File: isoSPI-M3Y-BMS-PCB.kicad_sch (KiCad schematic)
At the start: 439 parts, among them J1 Screw_Terminal_01x04, J10 Screw_Terminal_01x04, J11 Screw_Terminal_01x03, J12 Screw_Terminal_01x08, J13 Conn_02x10_Odd_Even, J14 Screw_Terminal_01x04, J15 USB_C_Receptacle_USB2.0_16P, J16 Conn_01x03, J17 USB_C_Receptacle_USB2.0_16P, J18 USB_C_Receptacle_USB2.0_16P, J2 Conn_02x10_Odd_Even, J3 8P8C_LED_Shielded_x2, J5 OEM Shunt Connector, J6 349128020, J7 OEM HV Sense Connector, J8 OEM Connector, J9 Conn_01x03, K10 FC Positive, K11 FC Negative, K12 Link Negative, K13 Inverter, K14 Link Positive, K15 Link Negative, K16 FC Positive, K17 FC Negative, K18 Inverter, K9 Link Positive, Q1 CRSM034N06L2, Q2 CRSM034N06L2, Q3 CRSM034N06L2, Q5 CRSM034N06L2, SW1 TS-1187A-B-A-B, SW2 TS-1187A-B-A-B, SW3 TS-1187A-B-A-B, SW4 TS-1187A-B-A-B, U1 SN74LV1T08DBVR, U10 LTV-217-B-G, U11 RP2354B, U12 ADS1115, U13 ISO1050DUB, U15 SN74LV1T08DBVR, U16 BatMan, U17 TPS5430DDAR, U2 ISO1540, U20 LTV-217-B-G, U21 AMS1117-3.3, U22 F0505S-1WR3, U23 SN74LV1T08DBVR, U24 F0505S-1WR3, U25 SN74LV1T08DBVR, U26 SN74LV1T08DBVR, U27 RP2354B, U28 AM26LV32EIDR, U29 B0505S-3WR2, U3 INA228, U30 ISO1540, U32 SP3485EN-L/TR, U4 ISO1540, U5 LTV-217-B-G, U6 F0505S-1WR3, U7 LTV-217-B-G, U8 LTV-217-B-G, U9 LTV-217-B-G, Y1 ABM8-272-T3, Y2 ABM8-272-T3

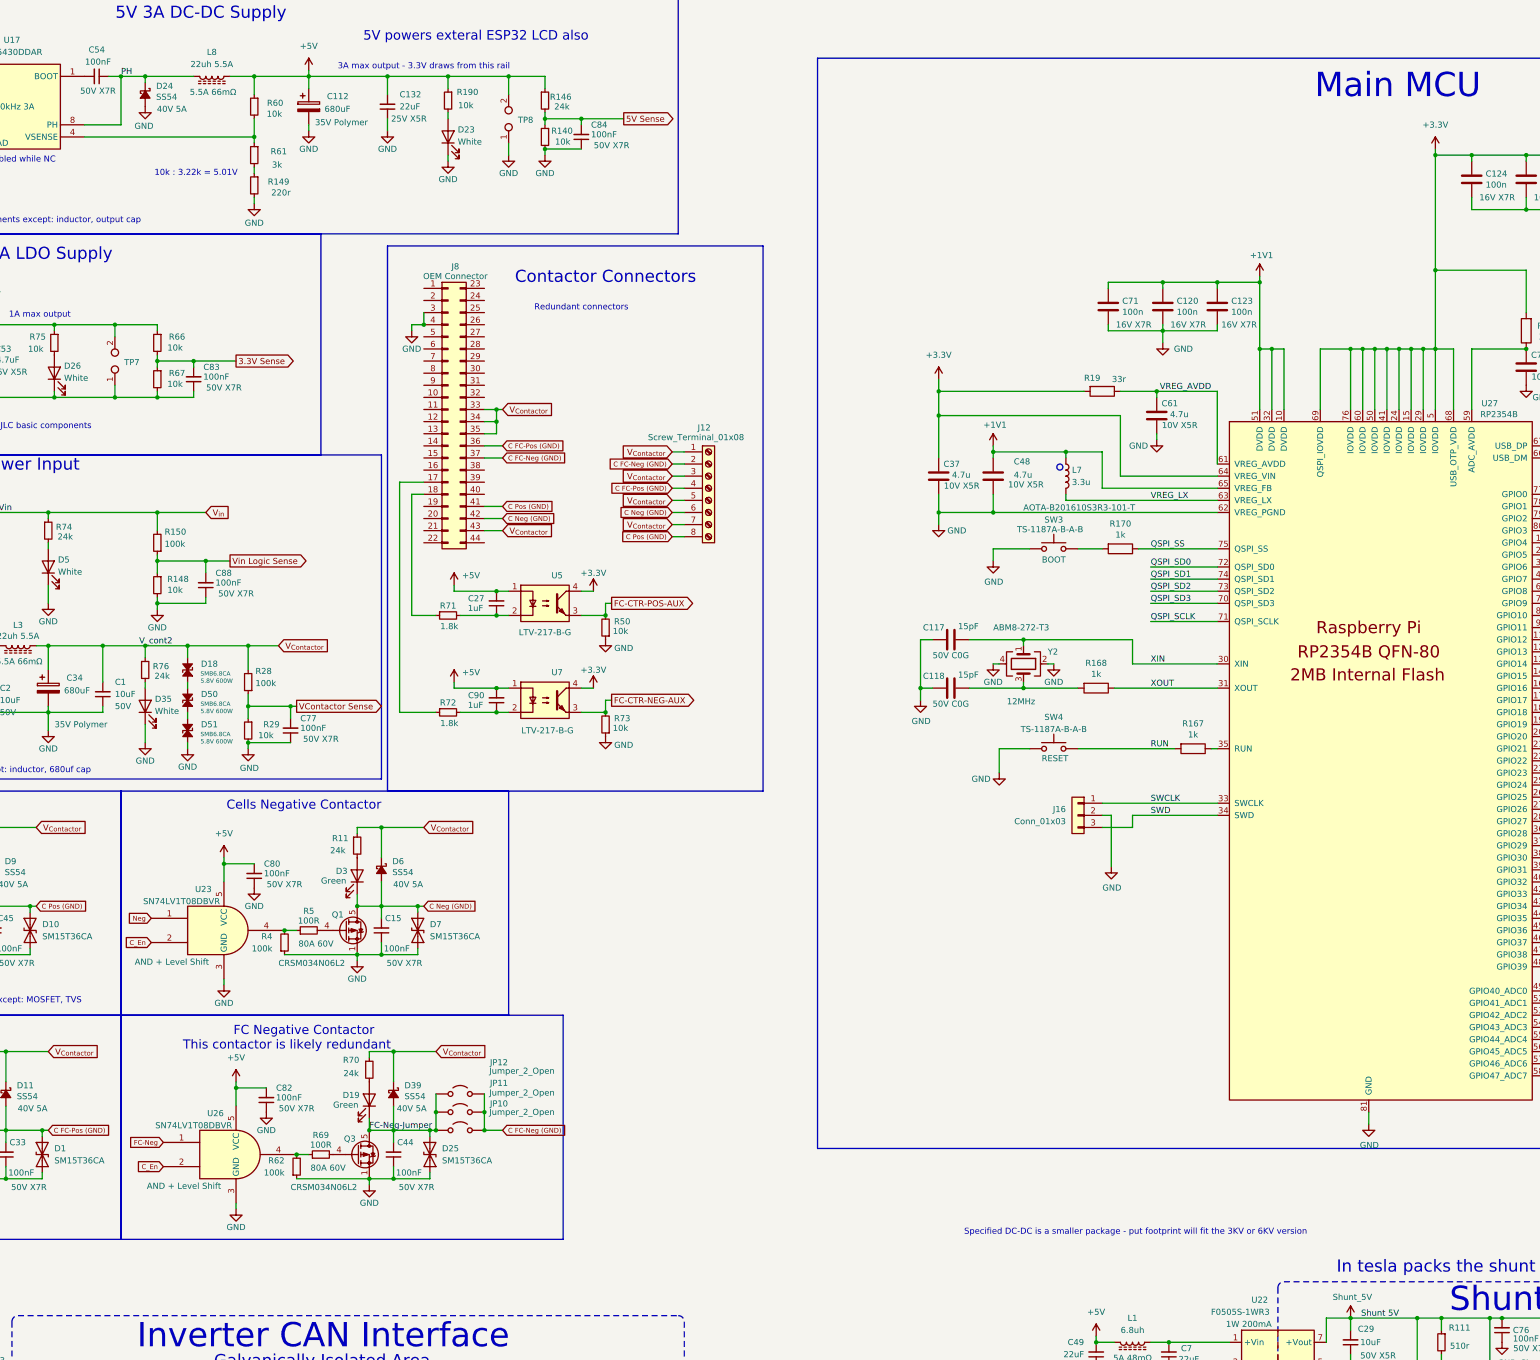
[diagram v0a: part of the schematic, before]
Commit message: routed dc-dc
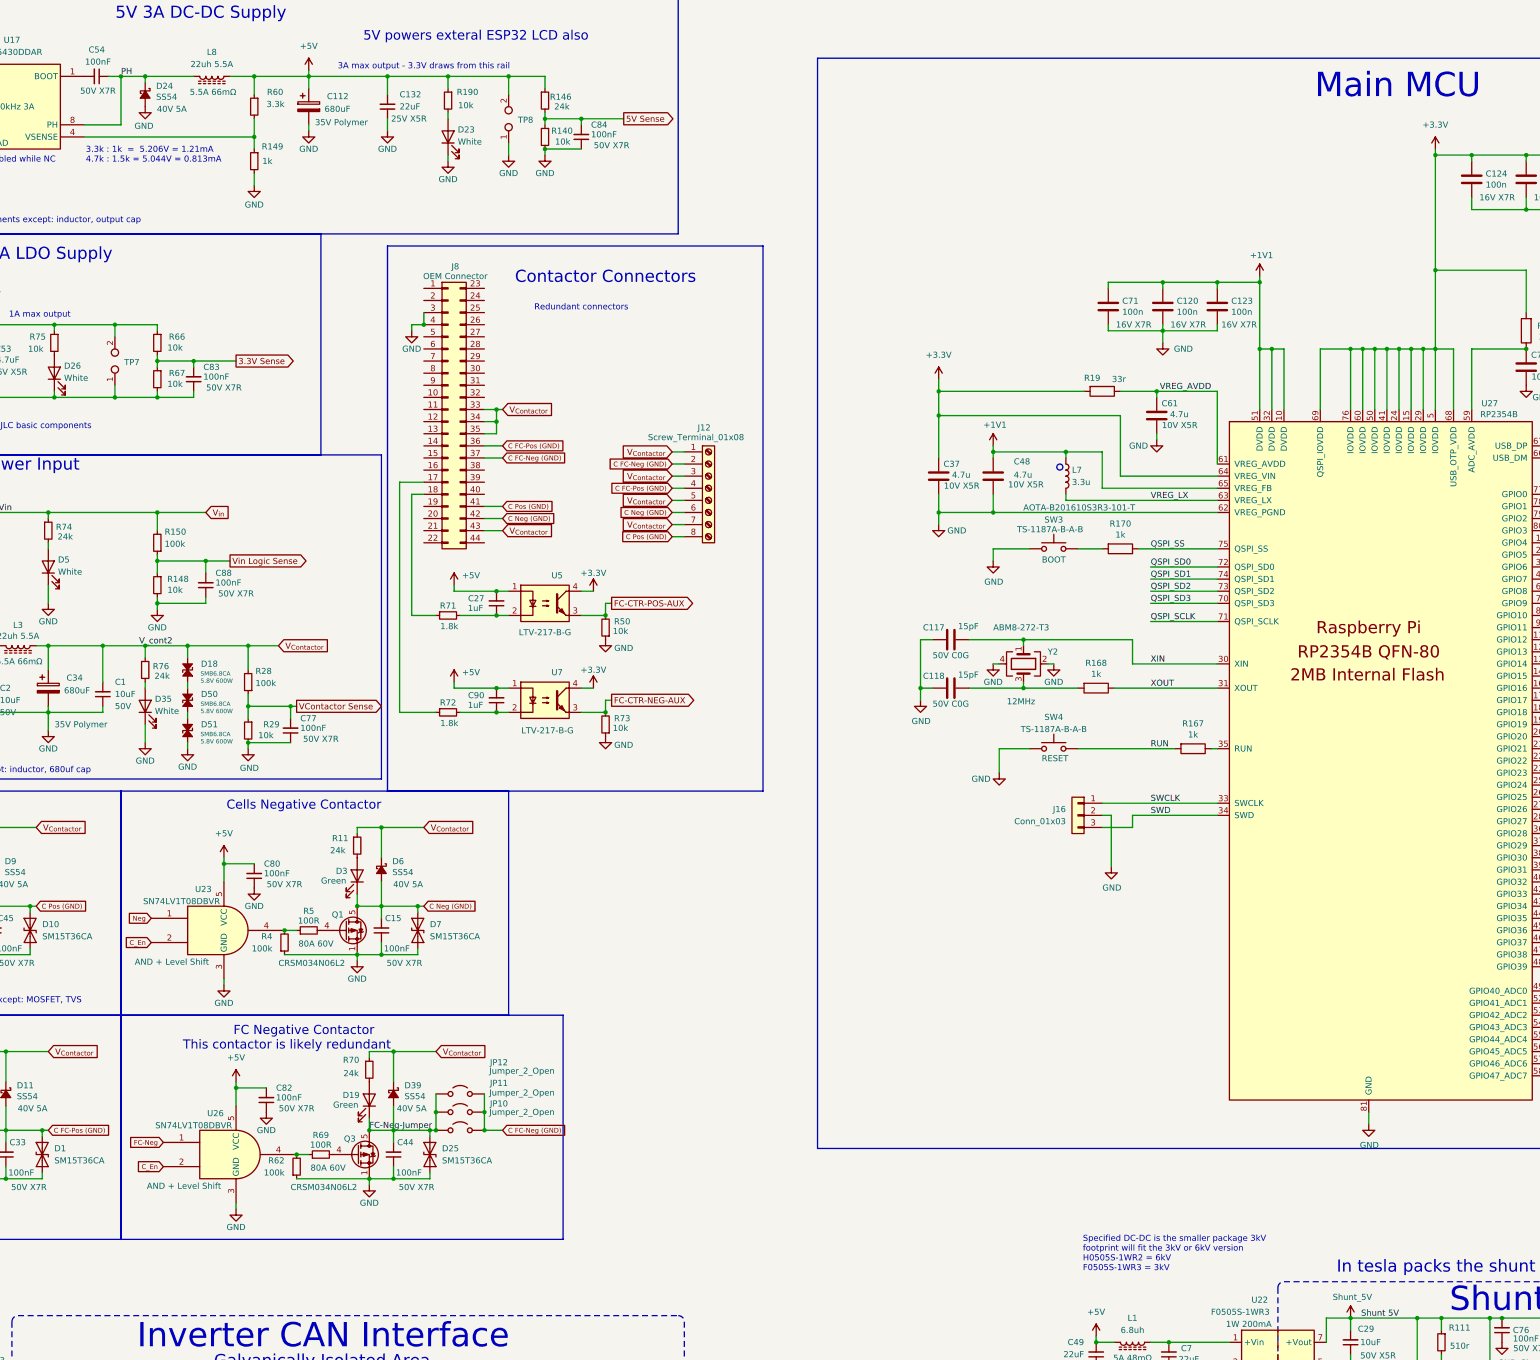
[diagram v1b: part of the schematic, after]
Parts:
- removed R61: 3k, Resistor_SMD:R_0603_1608Metric, symbol Device:R_Small
- R149: value 220r -> 1k; footprint Resistor_SMD:R_0603_1608Metric -> Resistor_SMD:R_0402_1005Metric; JLCPCB Part # C22962 -> C11702
- R60: value 10k -> 3.3k; footprint Resistor_SMD:R_0603_1608Metric -> Resistor_SMD:R_0402_1005Metric; JLCPCB Part # C25804 -> C25890
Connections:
- net at R60.2, U17.4 (VSENSE): now also R149.1
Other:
- note added: "3.3k : 1k = 5.206V = 1.21mA 4.7k : 1.5k = 5.044V = 0.813mA"
- note added: "Specified DC-DC is the smaller package 3kV footprint will fit the 3kV or 6kV version H0505S-1WR2 = 6kV F0505S-1WR3 = 3kV"
- note removed: "10k : 3.22k = 5.01V"
- note removed: "Specified DC-DC is a smaller package - put footprint will fit the 3KV or 6KV version"
- moved on the sheet: R149
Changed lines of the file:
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@@
 		)
 	)
-	(text "Specified DC-DC is a smaller package - put footprint will fit the 3KV or 6KV version"
+	(text "Specified DC-DC is the smaller package 3kV\nfootprint will fit the 3kV or 6kV version\nH0505S-1WR2 = 6kV\nF0505S-1WR3 = 3kV\n"
 		(exclude_from_sim no)
-		(at 277.114 282.448 0)
+		(at 302.006 290.068 0)
 		(effects
 			(font
@@
 		)
 	)
-	(text "10k : 3.22k = 5.01V"
+	(text "3.3k : 1k  =  5.206V = 1.21mA\n4.7k : 1.5k = 5.044V = 0.813mA"
 		(exclude_from_sim no)
-		(at 116.078 59.69 0)
+		(at 92.964 55.88 0)
 		(effects
 			(font
 				(size 1.27 1.27)
 			)
+			(justify left)
 		)
 	)
@@
 	(wire
 		(pts
-			(xy 128.27 64.77) (xy 128.27 66.04)
+			(xy 128.27 59.69) (xy 128.27 62.23)
 		)
 		(stroke
@@
 	(wire
 		(pts
-			(xy 128.27 52.07) (xy 128.27 53.34)
+			(xy 128.27 52.07) (xy 128.27 54.61)
 		)
 		(stroke
@@
 	(wire
 		(pts
-			(xy 128.27 58.42) (xy 128.27 59.69)
-		)
-		(stroke
-			(width 0)
-			(type default)
-		)
-	)
-	(wire
-		(pts
 			(xy 646.43 358.14) (xy 652.78 358.14)
 		)
@@
 	)
 	(symbol
-		(lib_id "Device:R_Small")
-		(at 128.27 55.88 0)
-		(mirror y)
-		(unit 1)
-		(exclude_from_sim no)
-		(in_bom yes)
-		(on_board yes)
-		(dnp no)
-		(property "Reference" "R61"
-			(at 135.128 55.118 0)
-			(effects
-				(font
-					(size 1.27 1.27)
-				)
-				(justify left)
-			)
-		)
-		(property "Value" "3k"
-			(at 134.112 57.912 0)
-			(effects
-				(font
-					(size 1.27 1.27)
-				)
-				(justify left)
-			)
-		)
-		(property "Footprint" "Resistor_SMD:R_0603_1608Metric"
-			(at 128.27 55.88 0)
-			(effects
-				(font
-					(size 1.27 1.27)
-				)
-				(hide yes)
-			)
-		)
-		(property "Datasheet" ""
-			(at 128.27 55.88 0)
-			(effects
-				(font
-					(size 1.27 1.27)
-				)
-				(hide yes)
-			)
-		)
-		(property "Description" ""
-			(at 128.27 55.88 0)
-			(effects
-				(font
-					(size 1.27 1.27)
-				)
-				(hide yes)
-			)
-		)
-		(property "JLCPCB Part #" "C4211"
-			(at 128.27 55.88 0)
-			(effects
-				(font
-					(size 1.27 1.27)
-				)
-				(hide yes)
-			)
-		)
-		(pin "1"
-		)
-		(pin "2"
-		)
-		(instances
-			(project "bms"
-				(path "/5d962221-5e0a-481f-afc5-67c7ec101fc1"
-					(reference "R61")
-					(unit 1)
-				)
-			)
-		)
-	)
-	(symbol
 		(lib_id "Device:C_Small")
 		(at 408.94 382.27 0)
@@
 	)
 	(symbol
+		(lib_id "Device:R_Small")
+		(at 128.27 45.72 0)
+		(mirror y)
+		(unit 1)
+		(exclude_from_sim no)
+		(in_bom yes)
+		(on_board yes)
+		(dnp no)
+		(property "Reference" "R60"
+			(at 134.366 42.672 0)
+			(effects
+				(font
+					(size 1.27 1.27)
+				)
+				(justify left)
+			)
+		)
+		(property "Value" "3.3k"
+			(at 134.62 45.212 0)
+			(effects
+				(font
+					(size 1.27 1.27)
+				)
+				(justify left)
+			)
+		)
+		(property "Footprint" "Resistor_SMD:R_0402_1005Metric"
+			(at 128.27 45.72 0)
+			(effects
+				(font
+					(size 1.27 1.27)
+				)
+				(hide yes)
+			)
+		)
+		(property "Datasheet" ""
+			(at 128.27 45.72 0)
+			(effects
+				(font
+					(size 1.27 1.27)
+				)
+				(hide yes)
+			)
+		)
+		(property "Description" ""
+			(at 128.27 45.72 0)
+			(effects
+				(font
+					(size 1.27 1.27)
+				)
+				(hide yes)
+			)
+		)
+		(property "JLCPCB Part #" "C25890"
+			(at 128.27 45.72 0)
+			(effects
+				(font
+					(size 1.27 1.27)
+				)
+				(hide yes)
+			)
+		)
+		(pin "1"
+		)
+		(pin "2"
+		)
+		(instances
+			(project "isoSPI-M3Y-BMS-PCB"
+				(path "/5d962221-5e0a-481f-afc5-67c7ec101fc1"
+					(reference "R60")
+					(unit 1)
+				)
+			)
+		)
+	)
+	(symbol
 		(lib_id "power:GND")
 		(at 389.89 304.8 0)
@@
 	(symbol
 		(lib_id "power:GND")
-		(at 128.27 66.04 0)
+		(at 128.27 62.23 0)
 		(unit 1)
 		(exclude_from_sim no)
@@
 		(dnp no)
 		(property "Reference" "#PWR058"
-			(at 128.27 72.39 0)
+			(at 128.27 68.58 0)
 			(effects
 				(font
@@
 		)
 		(property "Value" "GND"
-			(at 128.27 70.104 0)
+			(at 128.27 66.294 0)
 			(effects
 				(font
@@
 		)
 		(property "Footprint" ""
-			(at 128.27 66.04 0)
+			(at 128.27 62.23 0)
 			(effects
 				(font
@@
 		)
 		(property "Datasheet" ""
-			(at 128.27 66.04 0)
+			(at 128.27 62.23 0)
 			(effects
 				(font
@@
 		)
 		(property "Description" "Power symbol creates a global label with name \"GND\" , ground"
-			(at 128.27 66.04 0)
+			(at 128.27 62.23 0)
 			(effects
 				(font
@@
 	(symbol
 		(lib_id "Device:R_Small")
-		(at 128.27 62.23 0)
+		(at 128.27 57.15 0)
 		(mirror y)
 		(unit 1)
@@
 		(dnp no)
 		(property "Reference" "R149"
-			(at 135.636 61.468 0)
+			(at 134.366 54.102 0)
 			(effects
 				(font
@@
 			)
 		)
-		(property "Value" "220r"
-			(at 135.89 63.754 0)
+		(property "Value" "1k"
+			(at 132.08 57.15 0)
 			(effects
 				(font
@@
 			)
 		)
-		(property "Footprint" "Resistor_SMD:R_0603_1608Metric"
-			(at 128.27 62.23 0)
+		(property "Footprint" "Resistor_SMD:R_0402_1005Metric"
+			(at 128.27 57.15 0)
 			(effects
 				(font
@@
 		)
 		(property "Datasheet" ""
-			(at 128.27 62.23 0)
+			(at 128.27 57.15 0)
 			(effects
 				(font
@@
 		)
 		(property "Description" ""
-			(at 128.27 62.23 0)
+			(at 128.27 57.15 0)
 			(effects
 				(font
@@
 			)
 		)
-		(property "JLCPCB Part #" "C22962"
-			(at 128.27 62.23 0)
+		(property "JLCPCB Part #" "C11702"
+			(at 128.27 57.15 0)
 			(effects
 				(font
@@
 					(unit 1)
 				)
-			)
-		)
-	)
-	(symbol
-		(lib_id "Device:R_Small")
-		(at 128.27 45.72 0)
-		(mirror y)
-		(unit 1)
-		(exclude_from_sim no)
-		(in_bom yes)
-		(on_board yes)
-		(dnp no)
-		(property "Reference" "R60"
-			(at 134.366 44.958 0)
-			(effects
-				(font
-					(size 1.27 1.27)
-				)
-				(justify left)
-			)
-		)
-		(property "Value" "10k"
-			(at 134.112 47.244 0)
-			(effects
-				(font
-					(size 1.27 1.27)
-				)
-				(justify left)
-			)
-		)
-		(property "Footprint" "Resistor_SMD:R_0603_1608Metric"
-			(at 128.27 45.72 0)
-			(effects
-				(font
-					(size 1.27 1.27)
-				)
-				(hide yes)
-			)
-		)
-		(property "Datasheet" "~"
-			(at 128.27 45.72 0)
-			(effects
-				(font
-					(size 1.27 1.27)
-				)
-				(hide yes)
-			)
-		)
-		(property "Description" "Resistor, small symbol"
-			(at 128.27 45.72 0)
-			(effects
-				(font
-					(size 1.27 1.27)
-				)
-				(hide yes)
-			)
-		)
-		(property "JLCPCB Part #" "C25804"
-			(at 128.27 45.72 0)
-			(effects
-				(font
-					(size 1.27 1.27)
-				)
-				(hide yes)
-			)
-		)
-		(pin "1"
-		)
-		(pin "2"
-		)
-		(instances
-			(project "bms"
-				(path "/5d962221-5e0a-481f-afc5-67c7ec101fc1"
-					(reference "R60")
-					(unit 1)
-				)

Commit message: route ptc
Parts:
- added H6, H8: MountingHole_Pad, MountingHole:MountingHole_8.4mm_M8_Pad_Via, symbol Mechanical:MountingHole_Pad
- added JP15: SolderJumper_2_Open, Jumper:SolderJumper-2_P1.3mm_Open_RoundedPad1.0x1.5mm, symbol Jumper:SolderJumper_2_Open
- added R58: 1k, Resistor_SMD:R_0603_1608Metric, symbol Device:R_Small
- added R61: 510r, Resistor_SMD:R_0603_1608Metric, symbol Device:R_Small
- R141: JLCPCB Part # C23193 -> DNP
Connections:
- net +3.3V: now also JP15.2 (B)
- net C_En: now also JP15.1 (A), R58.2; no longer U11.13 (GPIO14)
- net Drive Unit Pos: now also H8.1
- net FC Pos: now also H6.1
- net GND_VSens: now also R61.2
- net HV Sense 5V: now also R61.1
- new net MCU2_GPIO14: R58.1, U11.13 (GPIO14)
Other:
- note added: "Manually solder if not installing supervisor MCU"

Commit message: added more ground pins
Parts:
- added TP22, TP23, TP24: TP, BMS_Library:TestPoint_THTPad_D1.5mm_Drill1.0mm, symbol Connector:TestPoint_Small
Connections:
- net GND: now also TP22.1, TP23.1
- net GND_Shunt: now also TP24.1

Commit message: lots of updates
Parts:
- removed R42: 1.8k, Resistor_SMD:R_0603_1608Metric, symbol Device:R_Small
- added C69: 680uF, Capacitor_THT:CP_Radial_D10.0mm_P5.00mm, symbol Device:C_Polarized
- added J19, J4: Conn_01x04, Connector_PinHeader_2.54mm:PinHeader_1x04_P2.54mm_Vertical, symbol Connector_Generic:Conn_01x04
- added J20: Screw_Terminal_01x04, Connector_Phoenix_MC:PhoenixContact_MC_1,5_4-G-3.81_1x04_P3.81mm_Horizontal, symbol Connector:Screw_Terminal_01x04
- added R78: 1k, Resistor_SMD:R_0603_1608Metric, symbol Device:R_Small
- added TP25, TP26, TP27, TP28, TP29, TP30: TP, BMS_Library:TestPoint_THTPad_D1.5mm_Drill1.0mm, symbol Connector:TestPoint_Small
- D1, D10, D25, D7: value SM15T36CA -> SMCJ33CA; Field6 (none) -> 33V 1.5kW; JLCPCB Part # C1976312 -> C224050
- J10: Field5 (none) -> 3.81P Screw Terminal
- J11: value Screw_Terminal_01x03 -> 3.81P Screw Terminal
- J12: value Screw_Terminal_01x08 -> 3.81P Screw Terminal
- J14: Field5 (none) -> 7.62mm Pitch Screw Terminal
- J6: Field6 (none) -> OEM Connector
- R23, R36, R38, R71, R72: value 1.8k -> 1k; JLCPCB Part # C4177 -> C21190
- R37, R39: value 1.8k -> 2.2k; JLCPCB Part # C4177 -> C4190
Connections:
- net C Neg (GND): now also D10.2 (A2); no longer D7.2 (A2)
- net C Pos (GND): now also D7.2 (A2); no longer D10.2 (A2)
- net CAN 5V: now also R39.2; no longer R37.2
- net Extra Output 1: now also R72.1; no longer R39.2
- net Extra Output 2: now also R38.1; no longer R38.2
- net GND: now also C69.2, J19.1 (Pin_1), J20.3 (Pin_3), J20.4 (Pin_4), J4.1 (Pin_1)
- net GND_RS: now also TP30.1
- net RUN: now also TP28.1
- net USB2_D+: now also J19.2 (Pin_2)
- net USB2_D-: now also J19.3 (Pin_3)
- net USB_D+: now also J4.2 (Pin_2)
- net USB_D-: now also J4.3 (Pin_3)
- net V_{in}: now also C69.1
- net at D30.2 (A), J17.A4 (VBUS), J17.A9 (VBUS)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: now also J19.4 (Pin_4)
- net at D53.2 (A), J18.A4 (VBUS), J18.A9 (VBUS)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: now also J4.4 (Pin_4)
- net FC-CTR-NEG-AUX-D: now reaches J8.17 (Pin_17)
- net FC-CTR-NEG-AUX-D: now also R71.1, J20.2 (Pin_2); no longer R72.1
- net at C90.1, U7.2: now also R71.2; no longer R72.2
- net at R49.2, SW1.2: now also TP25.1
- net at J3.24: now also R37.1
- net at J3.13, R36.2: now also R37.2
- net at R43.2, SW2.2: now also TP26.1
- net FC-CTR-POS-AUX-D: now reaches J8.18 (Pin_18)
- net FC-CTR-POS-AUX-D: now also J20.1 (Pin_1), R78.1; no longer R71.1
- net at C27.1, U5.2: now also R78.2; no longer R71.2
- net at U20.1: now also R38.2; no longer R38.1
- net at R39.1: now also J3.22; no longer U10.1
- net Serial API 5V Diode: now reaches D21.1 (K), J15.A4 (VBUS), J15.A9 (VBUS), J15.B4 (VBUS), J15.B9 (VBUS)
- net Serial API 5V Diode: now also TP29.1
- net at R170.2, SW3.2: now also TP27.1
- new net: R72.2, U10.1
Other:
- note added: "Aux Ret"
- note added: "Aux contacts inside of the FC contactors used to check for welding with or without energizing"
- note added: "DIY connector"
- note added: "PTC max current ~10A Under 1S charge time"
- note added: "Redundant connectors only one used at a time"
- moved on the sheet: C26, C40, C55, C57, C59, C60, C63, C64, C65, C66, C67, C74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
